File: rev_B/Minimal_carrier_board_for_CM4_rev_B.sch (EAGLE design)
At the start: 22 parts, among them IC1 MC74VHC1G14DFT1G, J1 P1-100, J2 P101-200, J6 629104190121

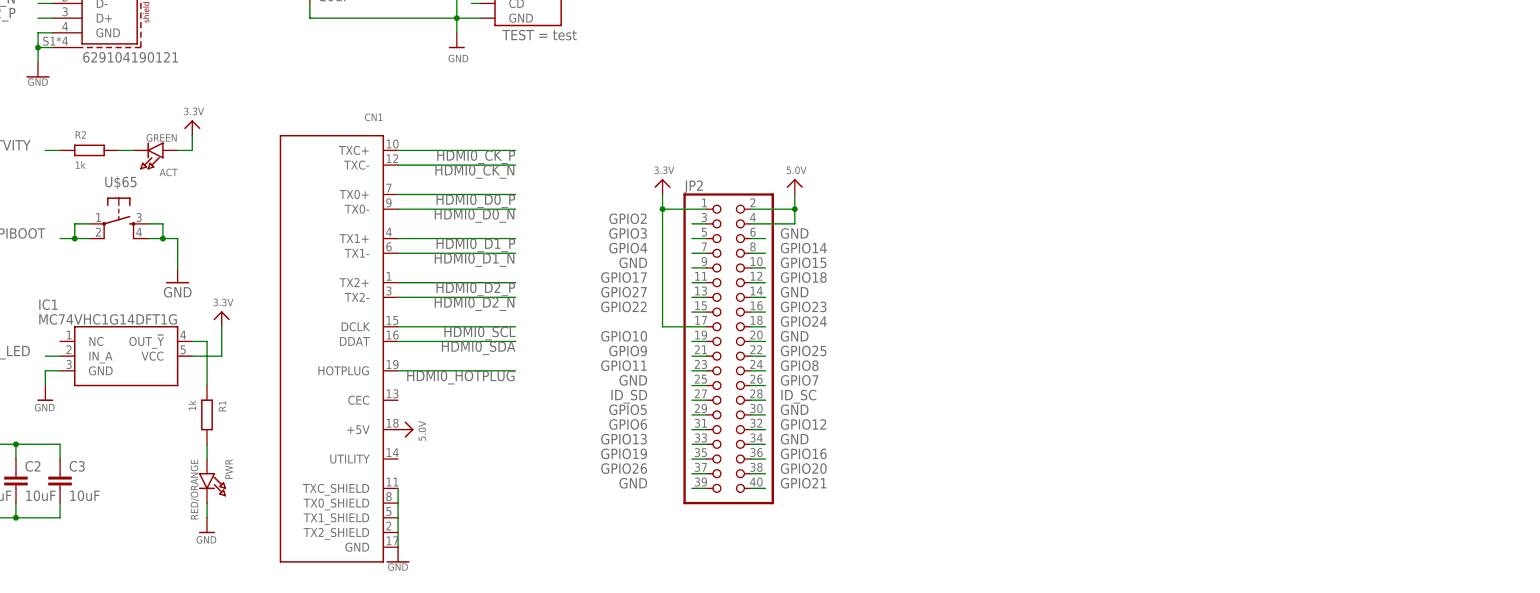
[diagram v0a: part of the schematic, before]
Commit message: Added connector for camera and DSI display
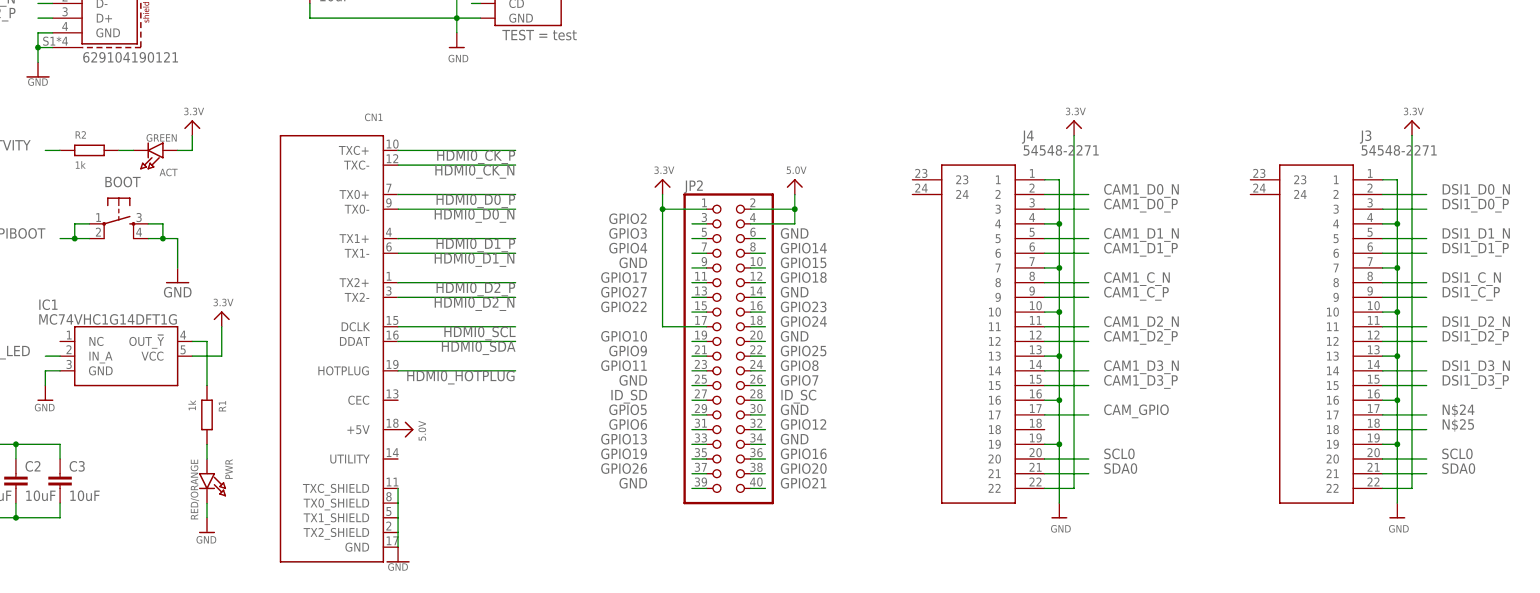
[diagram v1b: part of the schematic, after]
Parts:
- added J3, J4: 54548-2271, dronecz:54548-2271
- renumbered U$65 to BOOT
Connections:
- new net N$24: J3.17
- new net N$25: J3.18
- net 3.3V: now also J3.22, J4.22
- net CAM1_C_N: now also J4.8
- net CAM1_C_P: now also J4.9
- net CAM1_D0_N: now also J4.2
- net CAM1_D0_P: now also J4.3
- net CAM1_D1_N: now also J4.5
- net CAM1_D1_P: now also J4.6
- net CAM1_D2_N: now also J4.11
- net CAM1_D2_P: now also J4.12
- net CAM1_D3_N: now also J4.14
- net CAM1_D3_P: now also J4.15
- net CAM_GPIO: now also J4.17
- net DSI1_C_N: now also J3.8
- net DSI1_C_P: now also J3.9
- net DSI1_D0_N: now also J3.2
- net DSI1_D0_P: now also J3.3
- net DSI1_D1_N: now also J3.5
- net DSI1_D1_P: now also J3.6
- net DSI1_D2_N: now also J3.11
- net DSI1_D2_P: now also J3.12
- net DSI1_D3_N: now also J3.14
- net DSI1_D3_P: now also J3.15
- net GND: now also J3.1, J3.10, J3.13, J3.16, J3.19, J3.4, J3.7, J4.1, J4.10, J4.13, J4.16, J4.19, J4.4, J4.7
- net SCL0: now also J3.20, J4.20
- net SDA0: now also J3.21, J4.21

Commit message: Update
- moved USB-C, HDMI and USB-A connector to ensure that cables will not colide
- changed USB-C and HDMI connector to my library so I can display width od the connectors
- updated README accordingly
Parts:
- removed USB-C: TYPE-C-31-M-12, Custom-Parts:TYPE-C-31-M-12
- added J5: HRO_31_M_12_USB_C, dronecz:HRO_31_M_12_USB_C
- CN1: device microbuilder:HDMI_MOLEX_47151-0001 -> dronecz:HDMI_MOLEX_47151-0001
- J6: device Wurth_Connectors_WR-USB:629104190121 -> dronecz:629104190121
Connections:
- removed net N$8: R3.2, USB-C.CC1
- new net N$5: J5.CC1, R3.2
- net 5.0V: now also J5.VBUS; no longer USB-C.VBUS
- net GND: now also J5.GND, J5.SHIELD; no longer USB-C.GND, USB-C.TABS
- net N$3: now also J5.CC2; no longer USB-C.CC2
- net N$9: now also SD_CARD.CARD_DET; no longer SD_CARD.CD
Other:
- moved on the sheet: R3, R4
